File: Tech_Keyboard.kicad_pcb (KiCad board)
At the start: 2 copper layers, 41 parts, among them SW1 RotaryEncoder_Switch_MP, U1 MCU_Seeed_XIAO_RP2040

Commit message: Update Tech_Keyboard.kicad_pcb
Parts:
- moved S16 26.2 mm to (167.0, 104.2), turned to 0 degrees
- moved S18 26.2 mm to (205.1, 104.2), turned to 0 degrees
- moved D20 20.9 mm to (156.0, 29.2)
- moved D1 18.0 mm to (174.0, 29.0)
- moved D10 18.0 mm to (193.0, 67.2)
- moved D11 18.0 mm to (212.0, 67.2)
- moved D12 18.0 mm to (155.0, 86.2)
- moved D13 18.0 mm to (174.0, 86.2)
- moved D14 18.0 mm to (193.0, 86.2)
- moved D15 18.0 mm to (212.0, 86.2)
- moved D16 18.0 mm to (155.0, 105.2)
- moved D17 18.0 mm to (174.0, 105.2)
- moved D18 18.0 mm to (193.0, 105.2)
- moved D19 18.0 mm to (212.0, 105.2)
- moved D2 18.0 mm to (193.0, 29.2)
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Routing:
- net Column 0: track 0.00 -> 711.3 mm

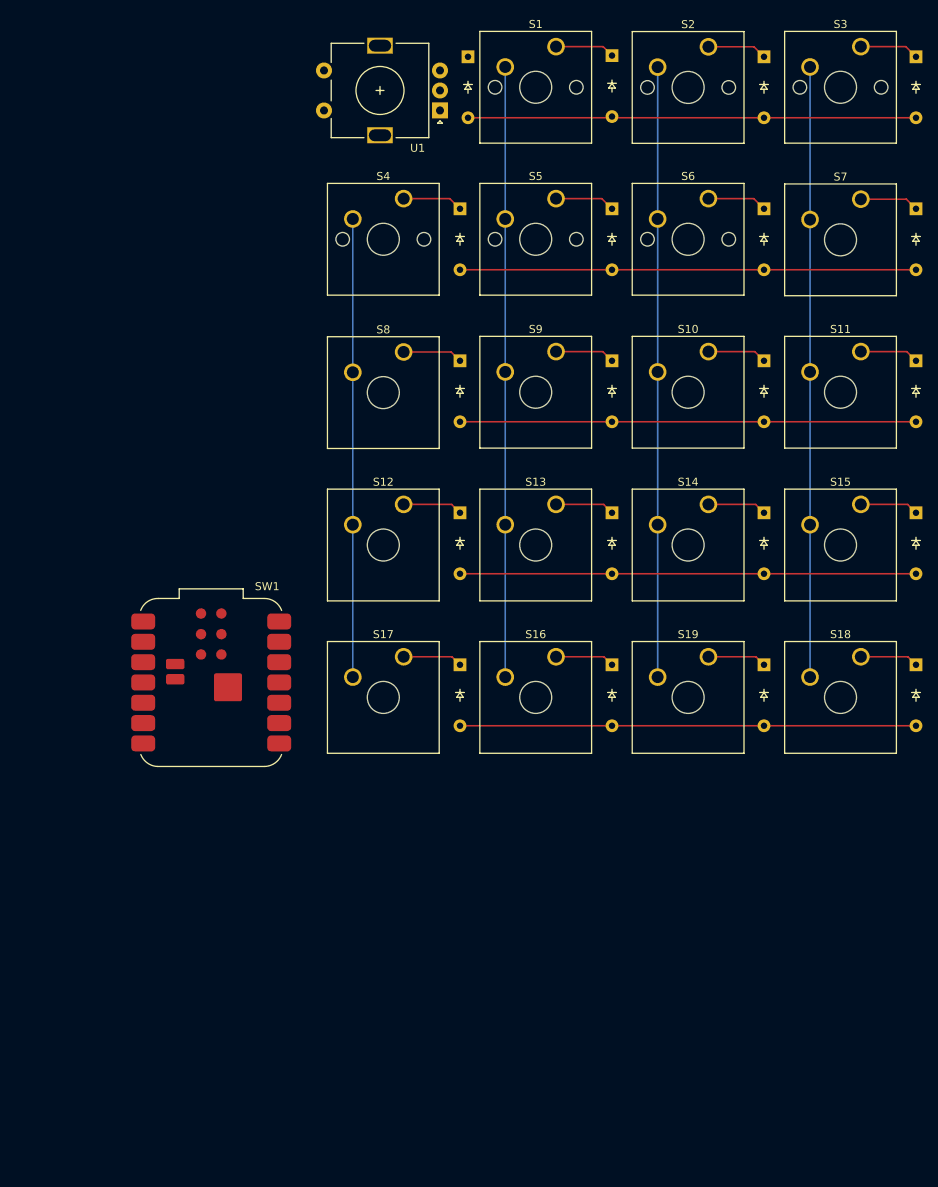
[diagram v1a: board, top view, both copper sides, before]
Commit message: New numpad layout and schematic and pcb
schematic and pcb fixed mostly. No wiring done yet on pcb again. Removed the push button the on the rotary encoder for simplicity due to overloading pin count.
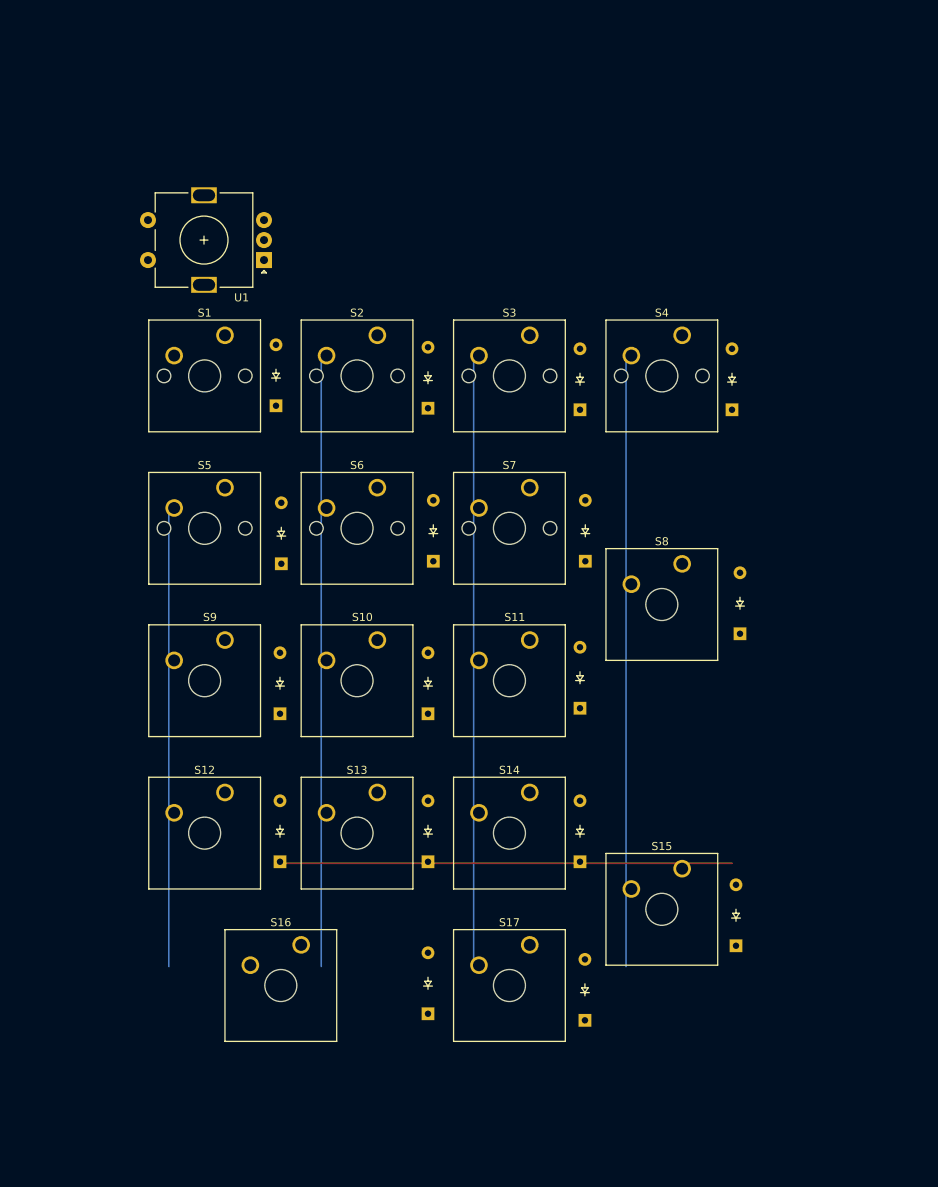
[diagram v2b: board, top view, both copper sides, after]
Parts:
- removed the D14 at (193.0, 86.2)
- removed D18, D20: ~, ScottoKeebs_Components:Diode_DO-35
- removed the S11 at (205.1, 66.0)
- removed the S17 at (148.0, 104.2)
- removed S19: ~, Button_Switch_Keyboard:SW_Cherry_MX_1.00u_Plate
- removed SW1: RotaryEncoder_Switch_MP, RF_Module:MCU_Seeed_ESP32C3
- added S1: ~, Button_Switch_Keyboard:SW_Cherry_MX_1.00u_PCB, F.Cu at (125.6, 64.0)
- S15: footprint Button_Switch_Keyboard:SW_Cherry_MX_1.00u_Plate -> Button_Switch_Keyboard:SW_Cherry_MX_2.00u_Vertical_Plate
- S16: footprint Button_Switch_Keyboard:SW_Cherry_MX_1.00u_Plate -> Button_Switch_Keyboard:SW_Cherry_MX_2.00u_Plate
- S8: renamed from S7; footprint Button_Switch_Keyboard:SW_Cherry_MX_1.00u_Plate -> Button_Switch_Keyboard:SW_Cherry_MX_2.00u_Vertical_Plate
- moved D9 101.5 mm to (132.5, 111.3), turned to 90 degrees
- moved D13 87.4 mm to (151.0, 129.8), turned to 90 degrees
- moved D12 87.1 mm to (132.5, 129.8), turned to 90 degrees
- moved D17 75.7 mm to (170.6, 149.6), turned to 90 degrees
- moved D16 66.7 mm to (151.0, 148.8), turned to 90 degrees
- moved D3 60.9 mm to (170.0, 73.3), turned to 90 degrees
- moved D2 60.8 mm to (151.0, 73.1), turned to 90 degrees
- moved D1 60.7 mm to (132.0, 72.8), turned to 90 degrees
- moved S17 54.9 mm to (163.7, 140.2)
- moved S8 50.8 mm to (182.8, 92.6)
- moved S15 50.7 mm to (182.8, 130.7)
- moved D5 49.7 mm to (132.7, 92.6), turned to 90 degrees
- moved D6 49.4 mm to (151.7, 92.2), turned to 90 degrees
- moved D7 49.4 mm to (170.7, 92.2), turned to 90 degrees
- moved S16 48.1 mm to (135.1, 140.2)
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- renumbered D8 to D10, D9 to D11, D10 to D12, D11 to D13, D12 to D14, D19 to D15, D13 to D16, D15 to D17, D16 to D4, D4 to D5, D5 to D6, D6 to D7, D17 to D8, D7 to D9, S9 to S10, S10 to S11, S18 to S17, S1 to S2, S2 to S3, S3 to S4, S4 to S5, S5 to S6, S6 to S7, S8 to S9
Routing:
- net Column 0: track 711.3 -> 343.1 mm

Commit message: wiring done
wired up pcb and fixed schematic... kind mad cuz i spent 3 hours and forgot to hit record...
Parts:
- added REF**: Stabilizer_MX_2.00u, ScottoKeebs_Stabilizer:Stabilizer_MX_2.00u, F.Cu at (180.2, 135.8)
- added REF**: Stabilizer_MX_2.00u, ScottoKeebs_Stabilizer:Stabilizer_MX_2.00u, F.Cu at (180.2, 97.7)
- added REF**: Stabilizer_MX_2.00u, ScottoKeebs_Stabilizer:Stabilizer_MX_2.00u, F.Cu at (132.6, 145.3)
- added SW2: RotaryEncoder, Rotary_Encoder:RotaryEncoder_Alps_EC11E_Vertical_H20mm, F.Cu at (172.9, 48.5)
- D1, D10, D11, D12, D13, D14, D15, D16, D17, D2, D3, D4, D5, D6, D7, D8, D9: moved to B.Cu
- U1: footprint Rotary_Encoder:RotaryEncoder_Alps_EC11E-Switch_Vertical_H20mm -> ScottoKeebs_MCU:Seeed_XIAO_RP2040
- moved U1 8.93 mm to (123.5, 49.1), turned to 0 degrees
- moved D17 1.46 mm to (170.0, 148.3)
- moved D7 1.26 mm to (169.5, 91.8)
- moved D13 1.00 mm to (152.0, 129.8)
- moved D15 0.93 mm to (189.5, 139.4)
- moved D4 0.83 mm to (189.7, 72.9)
- moved D16 0.81 mm to (151.6, 148.3)
- moved D5 0.81 mm to (132.6, 91.8)
- moved D3 0.79 mm to (170.7, 72.9)
- moved D10 0.70 mm to (151.6, 111.0)
- moved D2 0.66 mm to (151.6, 72.9)
- moved D11 0.61 mm to (169.5, 111.0)
- moved D1 0.50 mm to (132.5, 72.9)
- moved D6 0.50 mm to (151.6, 91.8)
- moved D9 0.35 mm to (132.6, 111.0)
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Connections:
- D1 pad 1: Column 0 -> Row 0
- D1 pad 2: Column 0 -> Row 0
- D10 pad 1: Column 0 -> Row 2
- D10 pad 2: Column 0 -> Row 2
- D11 pad 1: Column 0 -> Row 2
- D11 pad 2: Column 0 -> Row 2
- D12 pad 1: Column 0 -> Row 3
- D12 pad 2: Column 0 -> Row 3
- D13 pad 1: Column 0 -> Row 3
- D13 pad 2: Column 0 -> Row 3
- D14 pad 1: Column 0 -> Row 3
- D14 pad 2: Column 0 -> Row 3
- D15 pad 1: Column 0 -> Row 3
- D15 pad 2: Column 0 -> Row 3
- D16 pad 1: Column 0 -> Row 4
- D16 pad 2: Column 0 -> Row 4
- D17 pad 1: Column 0 -> Row 4
- D17 pad 2: Column 0 -> Row 4
- D2 pad 1: Column 0 -> Row 0
- D2 pad 2: Column 0 -> Row 0
- D3 pad 1: Column 0 -> Row 0
- D3 pad 2: Column 0 -> Row 0
- D4 pad 1: Column 0 -> Row 0
- D4 pad 2: Column 0 -> Row 0
- D5 pad 1: Column 0 -> Row 1
- D5 pad 2: Column 0 -> Row 1
- D6 pad 1: Column 0 -> Row 1
- D6 pad 2: Column 0 -> Row 1
- D7 pad 1: Column 0 -> Row 1
- D7 pad 2: Column 0 -> Row 1
- D8 pad 1: Column 0 -> Row 1
- D8 pad 2: Column 0 -> Row 1
- D9 pad 1: Column 0 -> Row 2
- D9 pad 2: Column 0 -> Row 2
- S1 pad 1: (no net) -> Column 0
- S1 pad 2: (no net) -> Row 0
- S10 pad 1: Column 0 -> Column 1
- S10 pad 2: Column 0 -> Row 2
- S11 pad 1: Column 0 -> Column 2
- S11 pad 2: Column 0 -> Row 2
- S12 pad 2: Column 0 -> Row 3
- S13 pad 1: Column 0 -> Column 1
- S13 pad 2: Column 0 -> Row 3
- S14 pad 1: Column 0 -> Column 2
- S14 pad 2: Column 0 -> Row 3
- S15 pad 1: Column 0 -> Column 3
- S15 pad 2: Column 0 -> Row 3
- S16 pad 2: Column 0 -> Row 4
- S17 pad 1: Column 0 -> Column 2
- S17 pad 2: Column 0 -> Row 4
- S2 pad 1: Column 0 -> Column 1
- S2 pad 2: Column 0 -> Row 0
- S3 pad 1: Column 0 -> Column 2
- S3 pad 2: Column 0 -> Row 0
- S4 pad 1: Column 0 -> Column 3
- S4 pad 2: Column 0 -> Row 0
- S5 pad 2: Column 0 -> Row 1
- S6 pad 1: Column 0 -> Column 1
- S6 pad 2: Column 0 -> Row 1
- S7 pad 1: Column 0 -> Column 2
- S7 pad 2: Column 0 -> Row 1
- S8 pad 1: Column 0 -> Column 3
- S8 pad 2: Column 0 -> Row 1
- S9 pad 2: Column 0 -> Row 2
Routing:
- net Column 0: track 343.1 -> 99.1 mm
- net Row 3: track 0.00 -> 243.0 mm
- net Row 4: track 0.00 -> 221.6 mm
- net Row 1: track 0.00 -> 169.7 mm
- net Row 0: track 0.00 -> 150.4 mm
- net Row 2: track 0.00 -> 148.0 mm
- net Column 3: track 0.00 -> 143.8 mm
- net Column 2: track 0.00 -> 132.9 mm
- net Column 1: track 0.00 -> 93.2 mm
- net GND: track 0.00 -> 48.3 mm
- net R0: track 0.00 -> 44.1 mm
- net R1: track 0.00 -> 43.1 mm
- added copper zone on B.Cu, net (none)
- added copper zone on F.Cu, net (none)
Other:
- board outline added: 82 x 119 mm

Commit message: 3D model being worked on, PCB finished
https://a360.co/41LIHIl
fusion 360 file
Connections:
- D1 pad 2: Row 0 -> Net-(D1-A)
- D10 pad 2: Row 2 -> Net-(D10-A)
- D11 pad 2: Row 2 -> Net-(D11-A)
- D12 pad 2: Row 3 -> Net-(D12-A)
- D13 pad 2: Row 3 -> Net-(D13-A)
- D14 pad 2: Row 3 -> Net-(D14-A)
- D15 pad 2: Row 3 -> Net-(D15-A)
- D16 pad 2: Row 4 -> Net-(D16-A)
- D17 pad 2: Row 4 -> Net-(D17-A)
- D2 pad 2: Row 0 -> Net-(D2-A)
- D3 pad 2: Row 0 -> Net-(D3-A)
- D4 pad 2: Row 0 -> Net-(D4-A)
- D5 pad 2: Row 1 -> Net-(D5-A)
- D6 pad 2: Row 1 -> Net-(D6-A)
- D7 pad 2: Row 1 -> Net-(D7-A)
- D8 pad 2: Row 1 -> Net-(D8-A)
- D9 pad 2: Row 2 -> Net-(D9-A)
- S1 pad 2: Row 0 -> Net-(D1-A)
- S10 pad 2: Row 2 -> Net-(D10-A)
- S11 pad 2: Row 2 -> Net-(D11-A)
- S12 pad 2: Row 3 -> Net-(D12-A)
- S13 pad 2: Row 3 -> Net-(D13-A)
- S14 pad 2: Row 3 -> Net-(D14-A)
- S15 pad 2: Row 3 -> Net-(D15-A)
- S16 pad 2: Row 4 -> Net-(D16-A)
- S17 pad 2: Row 4 -> Net-(D17-A)
- S2 pad 2: Row 0 -> Net-(D2-A)
- S3 pad 2: Row 0 -> Net-(D3-A)
- S4 pad 2: Row 0 -> Net-(D4-A)
- S5 pad 2: Row 1 -> Net-(D5-A)
- S6 pad 2: Row 1 -> Net-(D6-A)
- S7 pad 2: Row 1 -> Net-(D7-A)
- S8 pad 2: Row 1 -> Net-(D8-A)
- S9 pad 2: Row 2 -> Net-(D9-A)
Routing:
- net Row 0: track 150.4 -> 95.2 mm
- net Row 3: track 243.0 -> 188.4 mm
- net Row 1: track 169.7 -> 115.3 mm
- net Row 2: track 148.0 -> 107.6 mm
- net Row 4: track 221.6 -> 184.4 mm
- net Net-(D16-A): track 0.00 -> 23.7 mm
- net Net-(D5-A): track 0.00 -> 13.9 mm
- net Net-(D6-A): track 0.00 -> 13.9 mm
- net Net-(D8-A): track 0.00 -> 13.9 mm
- net Net-(D12-A): track 0.00 -> 13.9 mm
- net Net-(D4-A): track 0.00 -> 13.8 mm
- net Net-(D9-A): track 0.00 -> 13.8 mm
- net Net-(D3-A): track 0.00 -> 13.8 mm
- net Net-(D2-A): track 0.00 -> 13.8 mm
- net Net-(D13-A): track 0.00 -> 13.8 mm
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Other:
- board text added: "FALLOUT NUMPAD"
